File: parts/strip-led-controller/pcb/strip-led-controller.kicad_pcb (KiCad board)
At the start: 2 copper layers, 100 x 48 mm, 17 parts, among them J1 BUCK_IN, J2 PWR IN, J3 BUCK_OUT, SW2 SW_SPDT, U1 ESP32 Wemos D1 Mini

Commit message: change strip connectors to screw terminals
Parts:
- L1, L2: footprint Connector_PinHeader_2.54mm:PinHeader_1x04_P2.54mm_Horizontal -> TerminalBlock:TerminalBlock_Xinya_XY308-2.54-4P_1x04_P2.54mm_Horizontal
- moved L1 4.99 mm to (115.6, 37.1), turned to -90 degrees
- moved L2 4.99 mm to (115.6, 47.3), turned to -90 degrees
- moved ETH1 0.25 mm to (33.4, 48.9)
- moved ETH2 0.25 mm to (33.4, 28.6)
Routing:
- net GND: track 190.4 -> 0.00 mm
- net /12V: track 110.0 -> 0.00 mm, vias 1 -> 0
- net Net-(ETH2-RST): track 56.1 -> 0.00 mm, vias 1 -> 0
- net Net-(U1-IO_25): track 43.8 -> 0.00 mm, vias 1 -> 0
- net /3V3: track 40.5 -> 0.00 mm
- net /5V: track 28.6 -> 0.00 mm
- net Net-(U1-IO_27): track 27.8 -> 0.00 mm
- net Net-(ETH2-MISO): track 23.9 -> 0.00 mm
- net /MOSI: track 19.6 -> 0.00 mm
- net /SCK: track 18.7 -> 0.00 mm, vias 1 -> 0
- net /CS: track 14.5 -> 0.00 mm
- net /INT: track 14.0 -> 0.00 mm
- net +12V: track 8.56 -> 0.00 mm
- net Net-(L2-D1): track 7.34 -> 0.00 mm
- net Net-(L1-D1): track 7.34 -> 0.00 mm
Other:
- board text added: "Some kind of backflow diode might be a good idea on the strip connectors"
- board text added: "Strip Light Controller rev 1.3"
- board text removed: "Strip Light Controller rev 1.2.1"

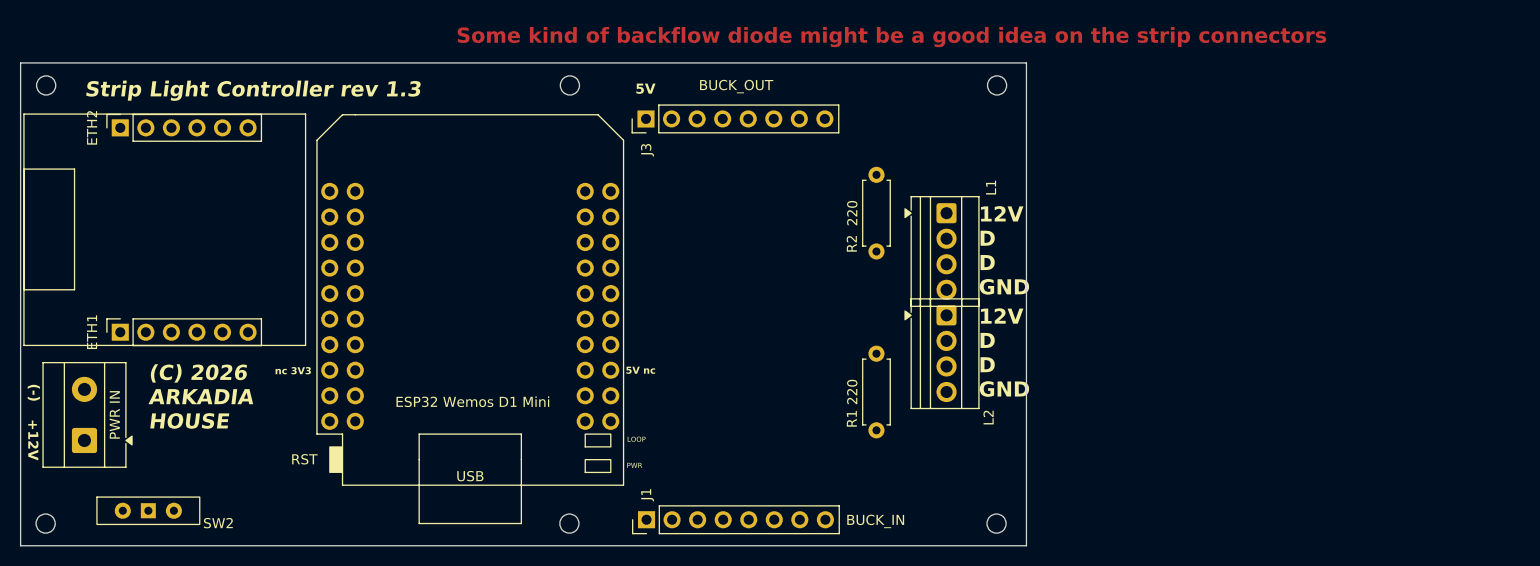
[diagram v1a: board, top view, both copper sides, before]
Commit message: update enclosure; update traces for higher amperage
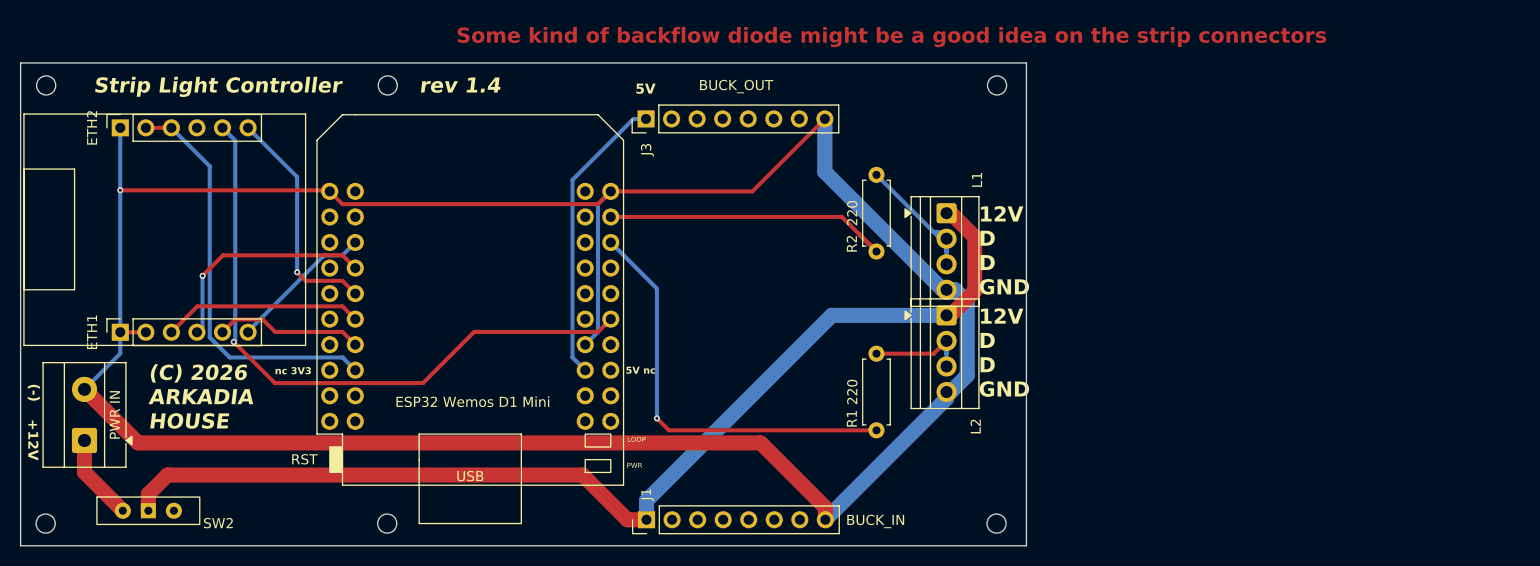
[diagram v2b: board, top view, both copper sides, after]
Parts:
- moved STANDOFF3 18.1 mm to (60.0, 24.4)
- moved STANDOF4 18.1 mm to (59.9, 68.0)
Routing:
- net GND: track 0.00 -> 252.7 mm, vias 0 -> 1
- net /12V: track 0.00 -> 106.3 mm
- net Net-(ETH2-RST): track 0.00 -> 63.7 mm, vias 0 -> 1
- net Net-(U1-IO_25): track 0.00 -> 41.7 mm, vias 0 -> 1
- net /3V3: track 0.00 -> 40.8 mm
- net Net-(U1-IO_27): track 0.00 -> 30.3 mm
- net /5V: track 0.00 -> 29.3 mm
- net Net-(ETH2-MISO): track 0.00 -> 23.0 mm, vias 0 -> 1
- net /SCK: track 0.00 -> 22.4 mm, vias 0 -> 1
- net /MOSI: track 0.00 -> 19.9 mm
- net Net-(L1-D1): track 0.00 -> 15.0 mm
- net /CS: track 0.00 -> 14.8 mm
- net /INT: track 0.00 -> 14.4 mm
- net Net-(L2-D1): track 0.00 -> 11.3 mm
- net +12V: track 0.00 -> 8.56 mm
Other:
- board text added: "Strip Light Controller"
- board text added: "rev 1.4"
- board text removed: "Strip Light Controller rev 1.3"
